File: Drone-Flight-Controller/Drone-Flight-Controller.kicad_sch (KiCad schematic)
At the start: 57 parts, among them J1 TestPoint, J10 TestPoint, J11 TestPoint, J12 TestPoint, J13 TestPoint, J2 TestPoint, J3 2044-2X20G00RA, J4 TestPoint, J5 TestPoint, J6 TestPoint, J7 TestPoint, J8 TestPoint, J9 TestPoint, SW1 TL3301NF160QG-KR, U1 MCP1700T-1802E/MB, U2 LMR51430, U3 ADC101C021CIMK, U4 ICM-20948, U5 BMP390, U6 PCA9685PW, U7 TXBN0304RUT

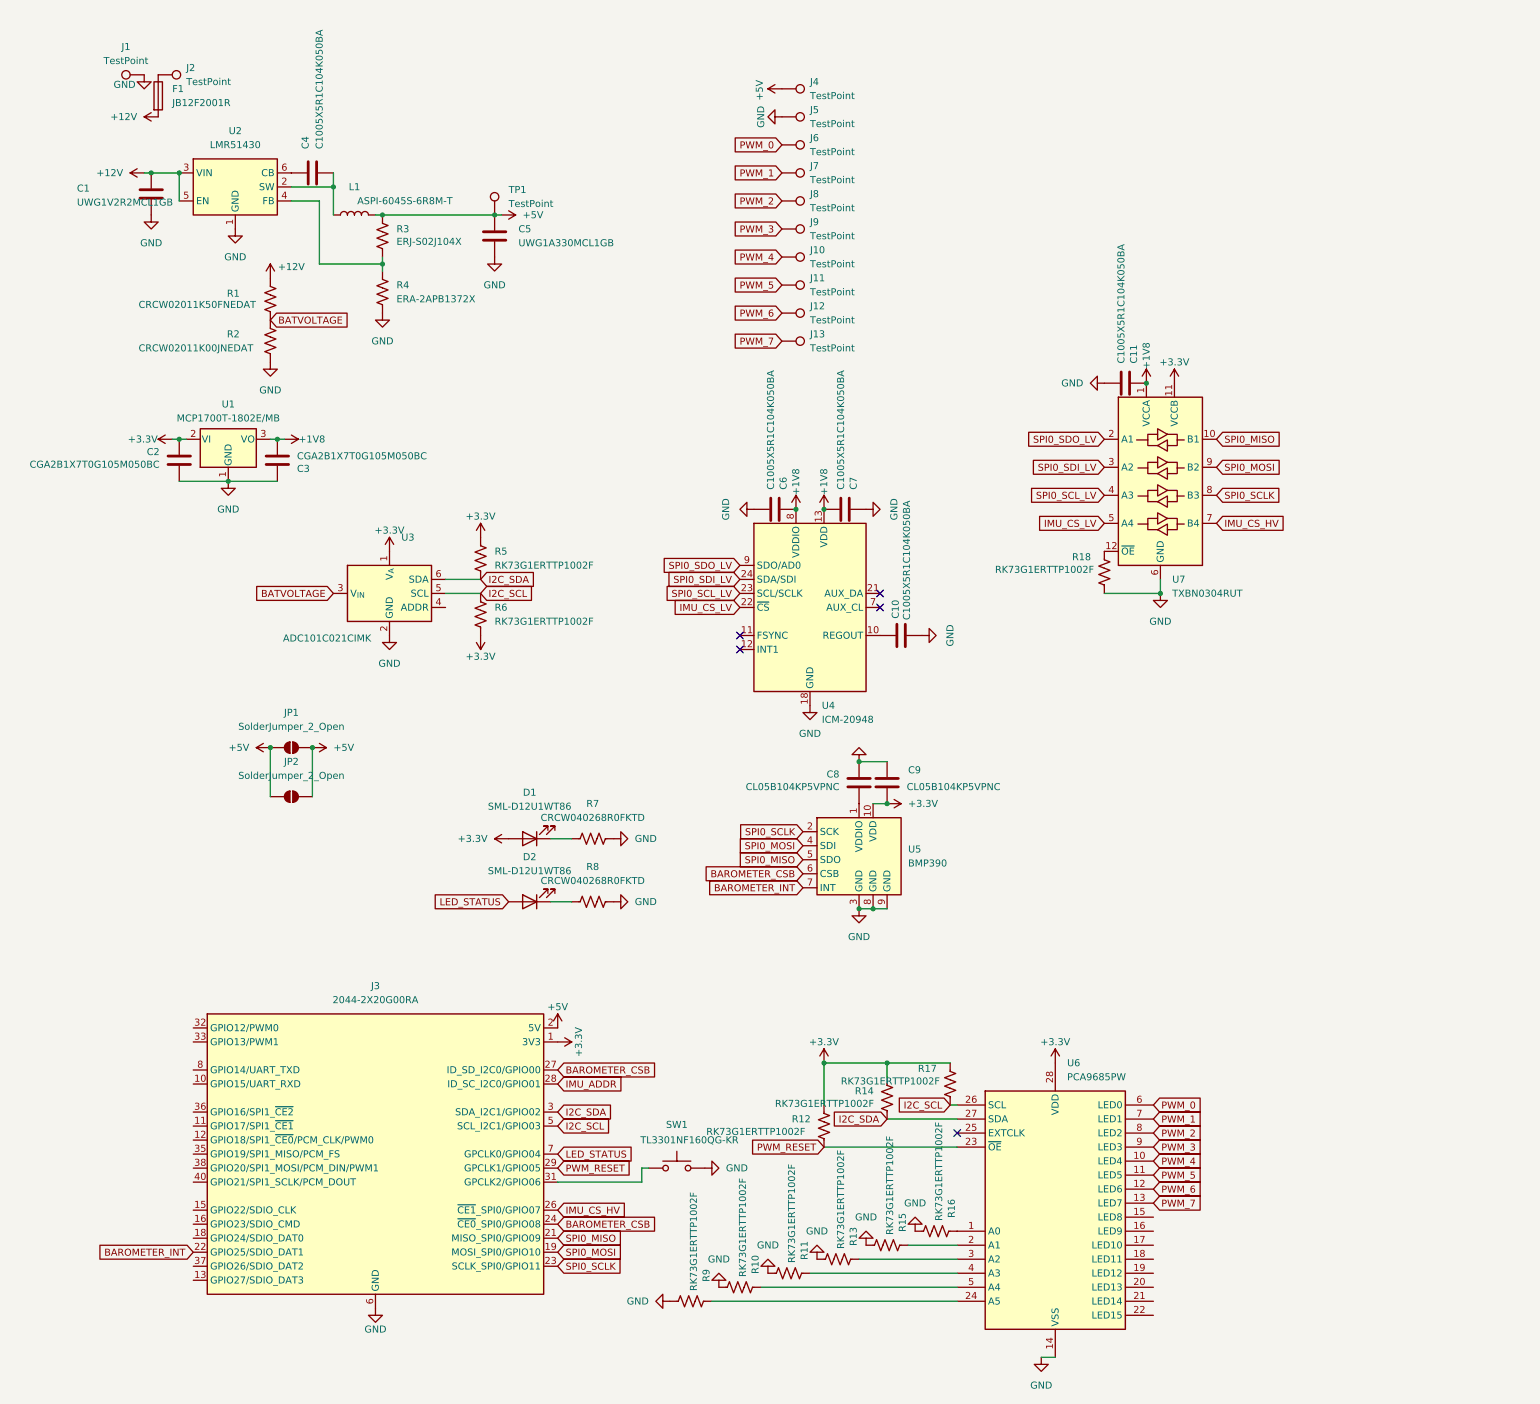
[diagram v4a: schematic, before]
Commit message: fix serial protocol
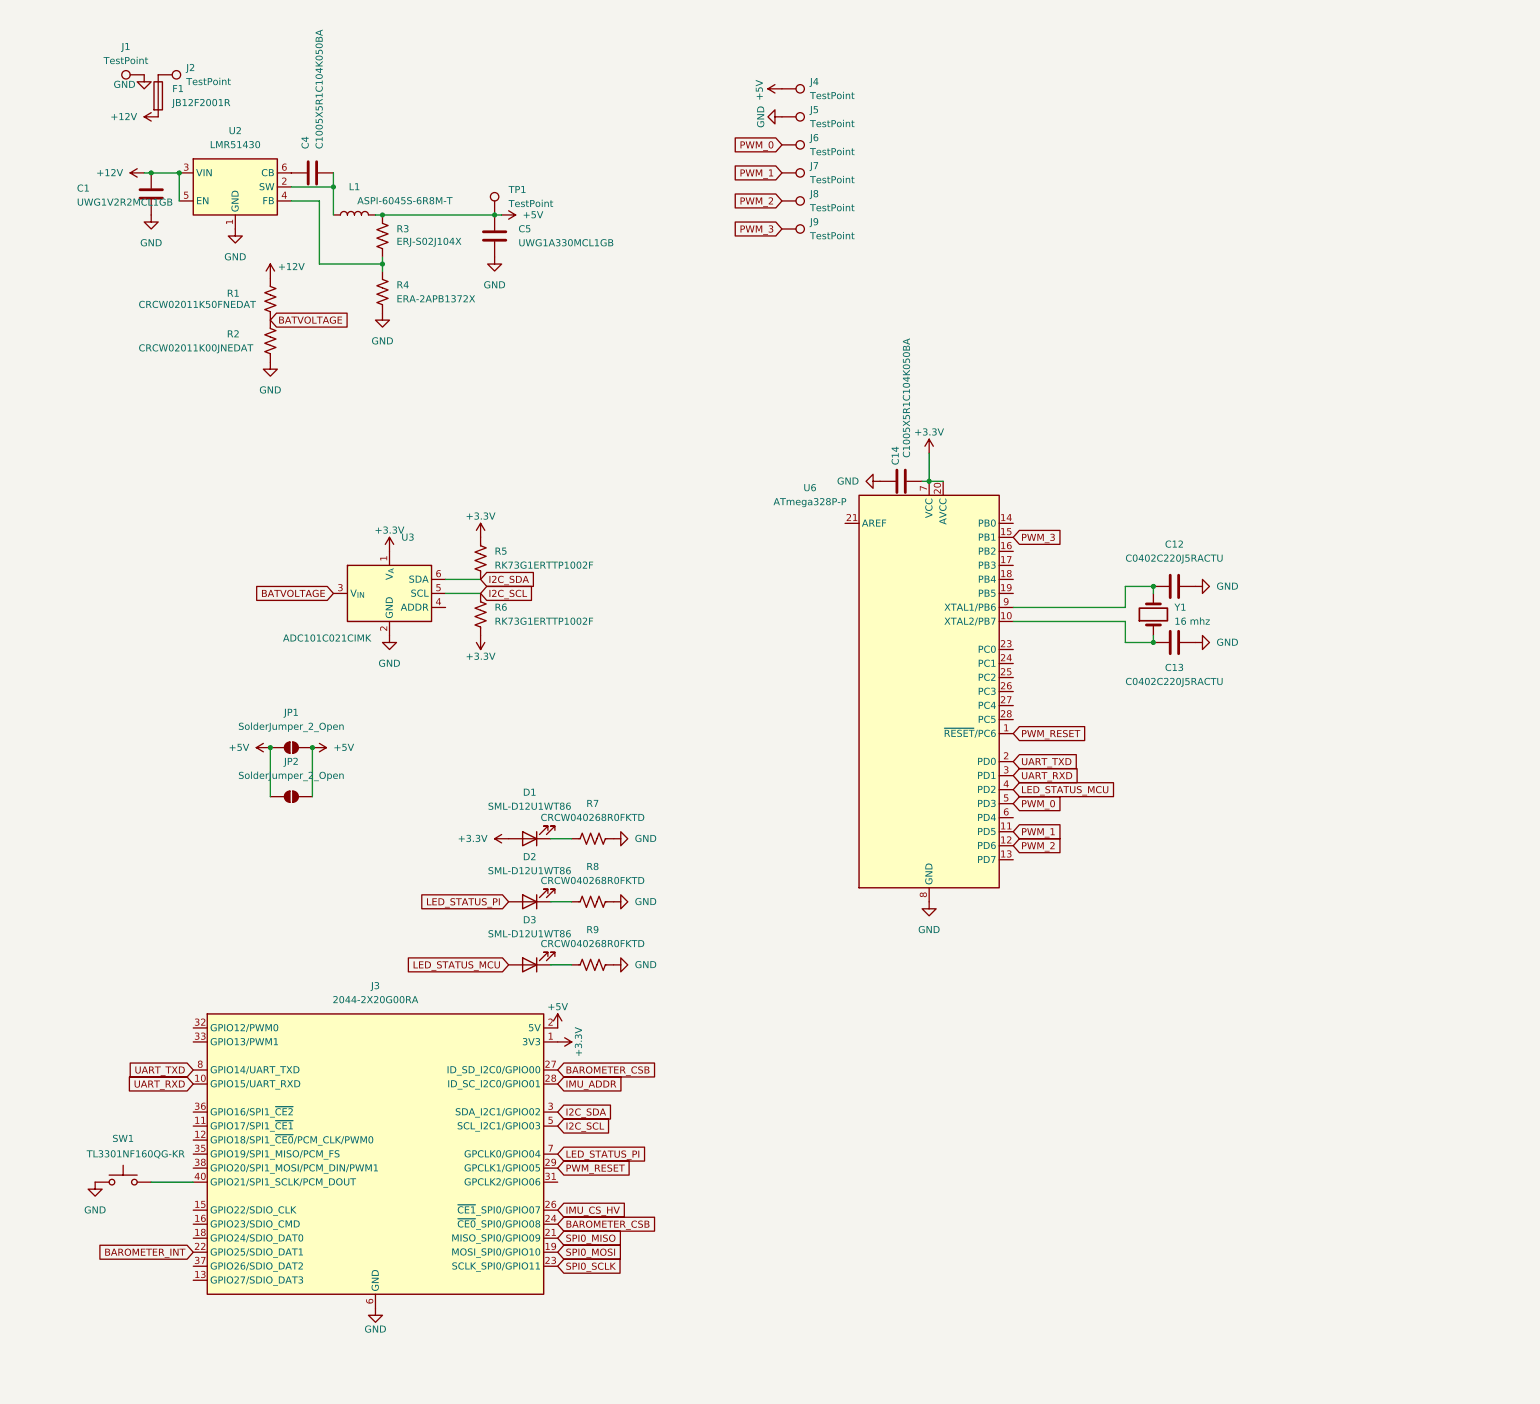
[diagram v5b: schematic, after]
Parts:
- removed C10, C11, C6, C7: C1005X5R1C104K050BA, Capacitor_SMD:C_0402_1005Metric, symbol Device:C
- removed C2, C3: CGA2B1X7T0G105M050BC, Capacitor_SMD:C_0402_1005Metric, symbol Device:C
- removed C8, C9: CL05B104KP5VPNC, Capacitor_SMD:C_0402_1005Metric, symbol Device:C
- removed J10, J11, J12, J13: TestPoint, TestPoint:TestPoint_Pad_D2.0mm, symbol Connector:TestPoint
- removed R10, R11, R12, R13, R14, R15, R16, R17, R18: RK73G1ERTTP1002F, Resistor_SMD:R_0402_1005Metric, symbol Device:R_US
- removed U1: MCP1700T-1802E/MB, Package_TO_SOT_SMD:SOT-89-3, symbol Regulator_Linear:MCP1700x-180xxMB
- removed U4: ICM-20948, Sensor_Motion:InvenSense_QFN-24_3x3mm_P0.4mm, symbol Sensor_Motion:ICM-20948
- removed U5: BMP390, Package_LGA:ST_HLGA-10_2x2mm_P0.5mm_LayoutBorder3x2y, symbol Sensor_Pressure:BMP390
- removed U6: PCA9685PW, Package_SO:TSSOP-28_4.4x9.7mm_P0.65mm, symbol Driver_LED:PCA9685PW
- removed U7: TXBN0304RUT, Package_DFN_QFN:Texas_R-PUQFN-N12, symbol Logic_LevelTranslator:TXBN0304RUT
- added C12, C13: C0402C220J5RACTU, Capacitor_SMD:C_0402_1005Metric, symbol Device:C
- added C14: C1005X5R1C104K050BA, Capacitor_SMD:C_0402_1005Metric, symbol Device:C
- added D3: SML-D12U1WT86, LED_SMD:LED_0603_1608Metric, symbol Device:LED
- added U6: ATmega328P-P, Package_DIP:DIP-28_W7.62mm, symbol MCU_Microchip_ATmega:ATmega328P-P
- added Y1: 16 mhz, Crystal:Crystal_SMD_Abracon_ABM3-2Pin_5.0x3.2mm, symbol Device:Crystal
- R9: value RK73G1ERTTP1002F -> CRCW040268R0FKTD
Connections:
- net +3.3V: now also C14.1, U6.20 (AVCC), U6.7 (VCC)
- net GND: now also SW1.1, C12.2, C13.2, C14.2, U6.22 (GND), U6.8 (GND); no longer SW1.2
- net PWM_0: now also U6.5 (PD3)
- net PWM_1: now also U6.11 (PD5)
- net PWM_2: now also U6.12 (PD6)
- net PWM_3: now also U6.15 (PB1)
- net PWM_RESET: now also U6.1 (~{RESET}/PC6)
- net UART_RXD: now reaches J3.10 (GPIO15/UART_RXD)
- net UART_RXD: now also U6.3 (PD1)
- net at J3.31 (GPCLK2/GPIO06): no longer SW1.1
- net at J3.40 (GPIO21/SPI1_SCLK/PCM_DOUT): now also SW1.2
- net UART_TXD: now reaches J3.8 (GPIO14/UART_TXD)
- net UART_TXD: now also U6.2 (PD0)
- net at R9.1: now also D3.1 (K)
- net LED_STATUS renamed LED_STATUS_PI
- new net: C13.1, U6.10 (XTAL2/PB7), Y1.1
- new net: C12.1, U6.9 (XTAL1/PB6), Y1.2
- new net LED_STATUS_MCU: D3.2 (A), U6.4 (PD2)
- no-connect marks 5 -> 0
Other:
- moved on the sheet: SW1

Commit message: add overlaid simulated horizon to video stream
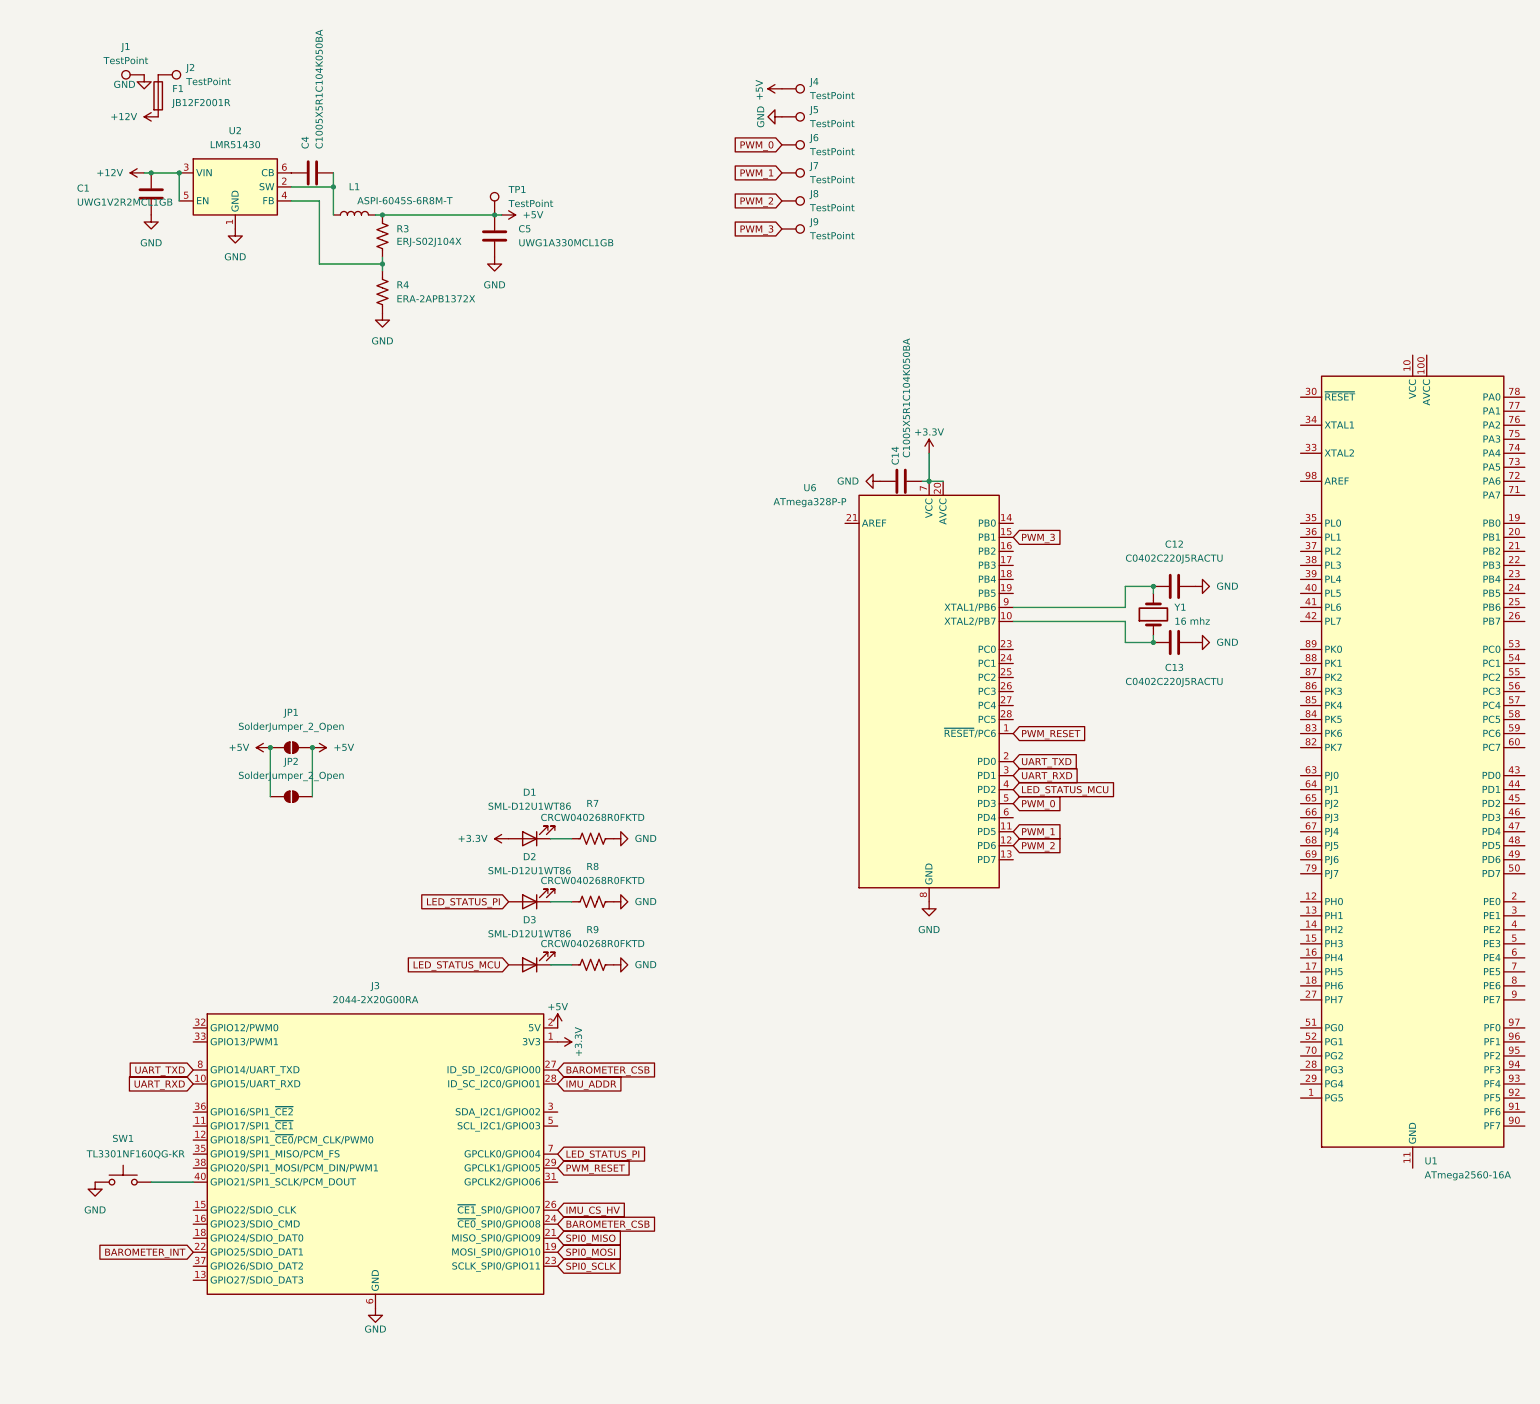
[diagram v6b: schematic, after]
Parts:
- removed R1: CRCW02011K50FNEDAT, Resistor_SMD:R_0402_1005Metric, symbol Device:R_US
- removed R2: CRCW02011K00JNEDAT, Resistor_SMD:R_0402_1005Metric, symbol Device:R_US
- removed R5, R6: RK73G1ERTTP1002F, Resistor_SMD:R_0402_1005Metric, symbol Device:R_US
- removed U3: ADC101C021CIMK, Package_TO_SOT_SMD:SOT-23-6, symbol Analog_ADC:ADC101C021CIMK
- added U1: ATmega2560-16A, Package_QFP:TQFP-100_14x14mm_P0.5mm, symbol MCU_Microchip_ATmega:ATmega2560-16A
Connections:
- net I2C_SCL: no longer names the net of J3.5 (SCL_I2C1/GPIO03)
- net I2C_SDA: no longer names the net of J3.3 (SDA_I2C1/GPIO02)
- new net: U1.10 (VCC), U1.31 (VCC), U1.61 (VCC), U1.80 (VCC)
- new net: U1.11 (GND), U1.32 (GND), U1.62 (GND), U1.81 (GND), U1.99 (GND)
